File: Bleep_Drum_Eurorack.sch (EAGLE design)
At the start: 62 parts, among them IC1 MCP6002, IC2 78L05Z, IC3 ATMEGA328P, IC4 MCP4921, Q1 2N3904, Q2 2N3904, Q3 2N3904, Q4 2N3904

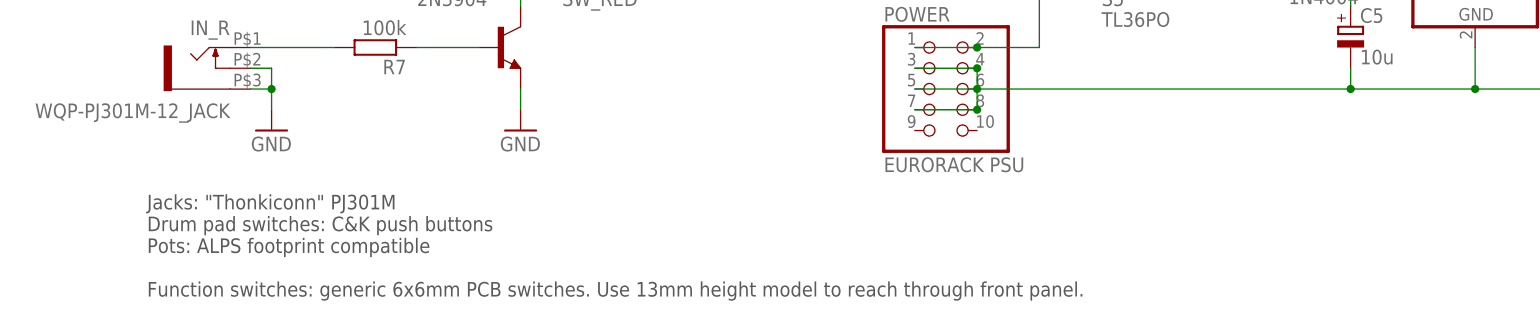
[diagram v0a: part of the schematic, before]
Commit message: Updated info text a bit.
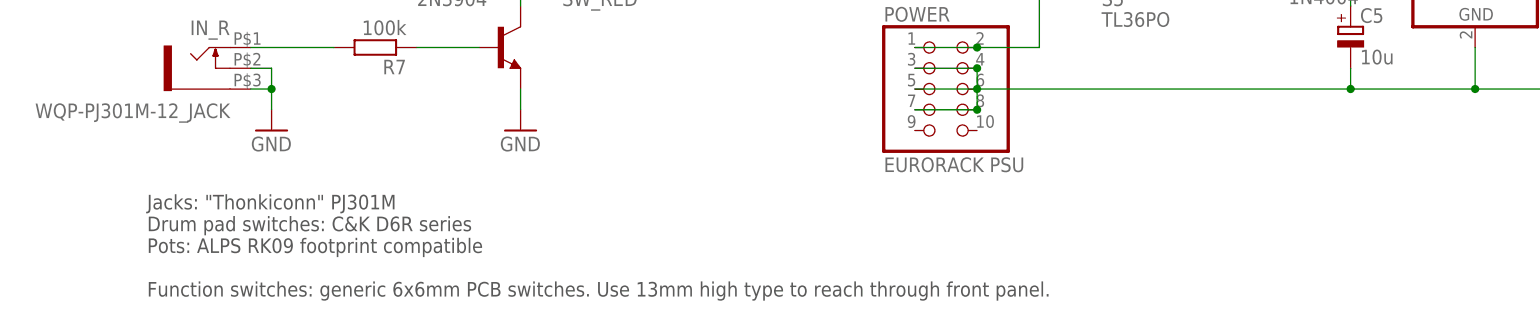
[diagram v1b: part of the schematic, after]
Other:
- note added: "Jacks: "Thonkiconn" PJ301M Drum pad switches: C&K D6R series Pots: ALPS RK09 footprint compatible Function switches: generic 6x6mm PCB switches. Use 13mm high type to reach through front panel."
- note removed: "Jacks: "Thonkiconn" PJ301M Drum pad switches: C&K push buttons Pots: ALPS footprint compatible Function switches: generic 6x6mm PCB switches. Use 13mm height model to reach through front panel."
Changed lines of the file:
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@@
 <text x="299.72" y="149.86" size="1.778" layer="91">Actually, RGB diode should be CC. </text>
 <text x="27.94" y="7.62" size="1.778" layer="97">Jacks: "Thonkiconn" PJ301M
-Drum pad switches: C&amp;K push buttons
-Pots: ALPS footprint compatible
-Function switches: generic 6x6mm PCB switches. Use 13mm height model to reach through front panel. </text>
+Drum pad switches: C&amp;K D6R series
+Pots: ALPS RK09 footprint compatible
+Function switches: generic 6x6mm PCB switches. Use 13mm high type to reach through front panel. </text>
 <text x="15.24" y="231.14" size="3.81" layer="97">Bleep Drum Eurorack
 CC BY-SA 2016 Lars Bengtsson

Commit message: R12=100kOhm.
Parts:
- R12: value 1M -> 100k
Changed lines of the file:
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@@
 <part name="Q4" library="transistor-npn" deviceset="2N3904" device=""/>
 <part name="R11" library="rcl" deviceset="R-EU_" device="0204/2V" value="1k"/>
-<part name="R12" library="rcl" deviceset="R-EU_" device="0204/2V" value="1M"/>
+<part name="R12" library="rcl" deviceset="R-EU_" device="0204/2V" value="100k"/>
 <part name="GND26" library="supply1" deviceset="GND" device=""/>
 <part name="OUT_AUDIO" library="thonkiconn" deviceset="WQP-PJ301M-12_JACK" device=""/>

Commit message: Changed ATmega328P into ATmega328. Arduino environment seems to expect the latter type (both work fine when programmed. It's just hard to get there with a "P" type chip :) ).
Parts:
- IC3: value ATMEGA328P -> ATMEGA328
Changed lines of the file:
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@@
 </classes>
 <parts>
-<part name="IC3" library="SparkFun-DigitalIC" deviceset="ATMEGA328P_PDIP" device="" value="ATMEGA328P"/>
+<part name="IC3" library="SparkFun-DigitalIC" deviceset="ATMEGA328P_PDIP" device="" value="ATMEGA328"/>
 <part name="FRAME1" library="frames" deviceset="A3L-LOC" device=""/>
 <part name="IC4" library="adafruit_mcp" deviceset="MCP4921" device="DIP8" value="MCP4921"/>
